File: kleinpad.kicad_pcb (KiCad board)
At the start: 2 copper layers, 79 x 79 mm, 31 parts, among them J1 Conn_01x02, J2 Conn_01x05, SW1 SW_Push, SW2 RotaryEncoder_Switch, U1 SuperMini nRF52840

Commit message: feat: add jlc order place
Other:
- board text added: "JLCJLCJLCJLC"
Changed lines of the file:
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@@
 		)
 		(embedded_fonts no)
+		(model "D:/kicad/kbd-3-final/kicad-packages3D/kbd.3dshapes/MX Series-Cherry Key.step"
+			(offset
+				(xyz 7.3 7.5 6)
+			)
+			(scale
+				(xyz 1 1 1)
+			)
+			(rotate
+				(xyz 90 -180 -0)
+			)
+		)
 	)
 	(footprint "kbd_Parts:Diode_TH_SMD"
@@
 			)
 			(justify left bottom mirror)
+		)
+	)
+	(gr_text "JLCJLCJLCJLC"
+		(at 123.8 63.8 0)
+		(layer "B.SilkS")
+		(effects
+			(font
+				(size 0.8 1)
+				(thickness 0.15)
+				(bold yes)
+			)
+			(justify left bottom mirror)

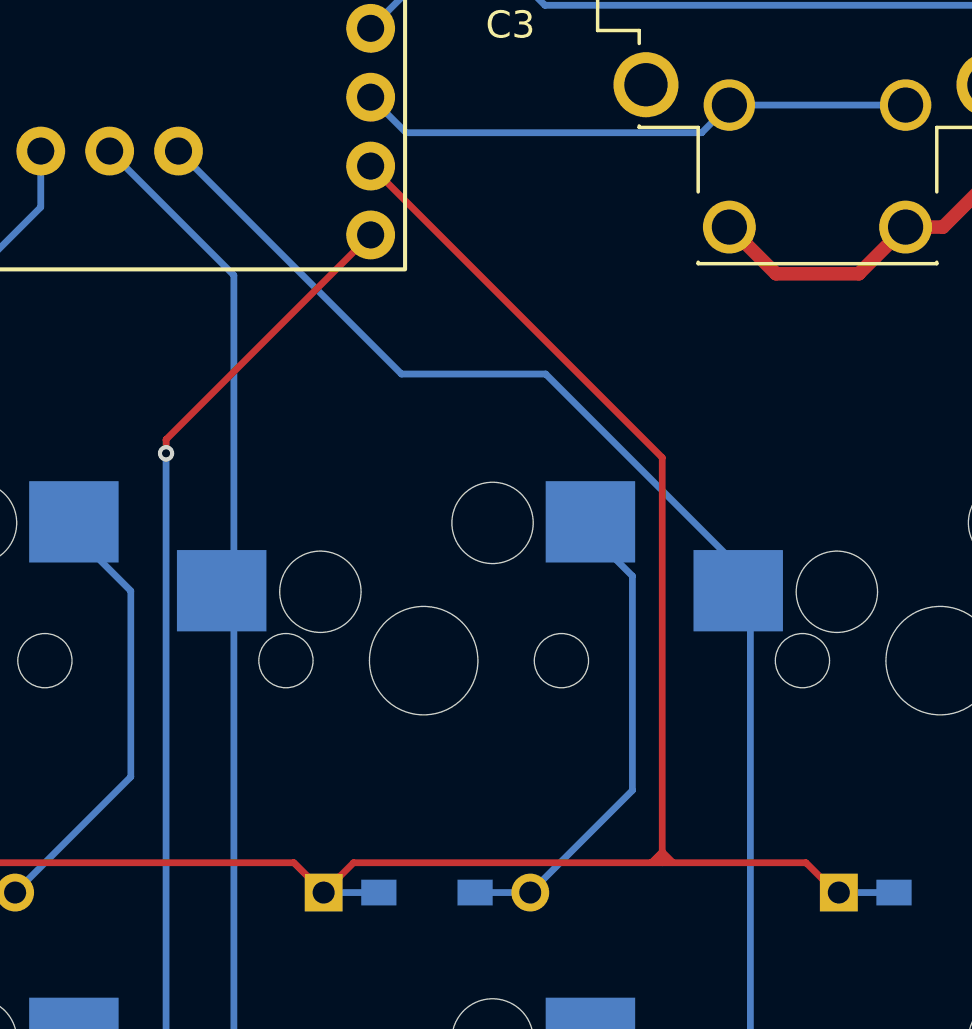
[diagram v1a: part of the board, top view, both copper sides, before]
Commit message: fix: 配線を少しだけ変更
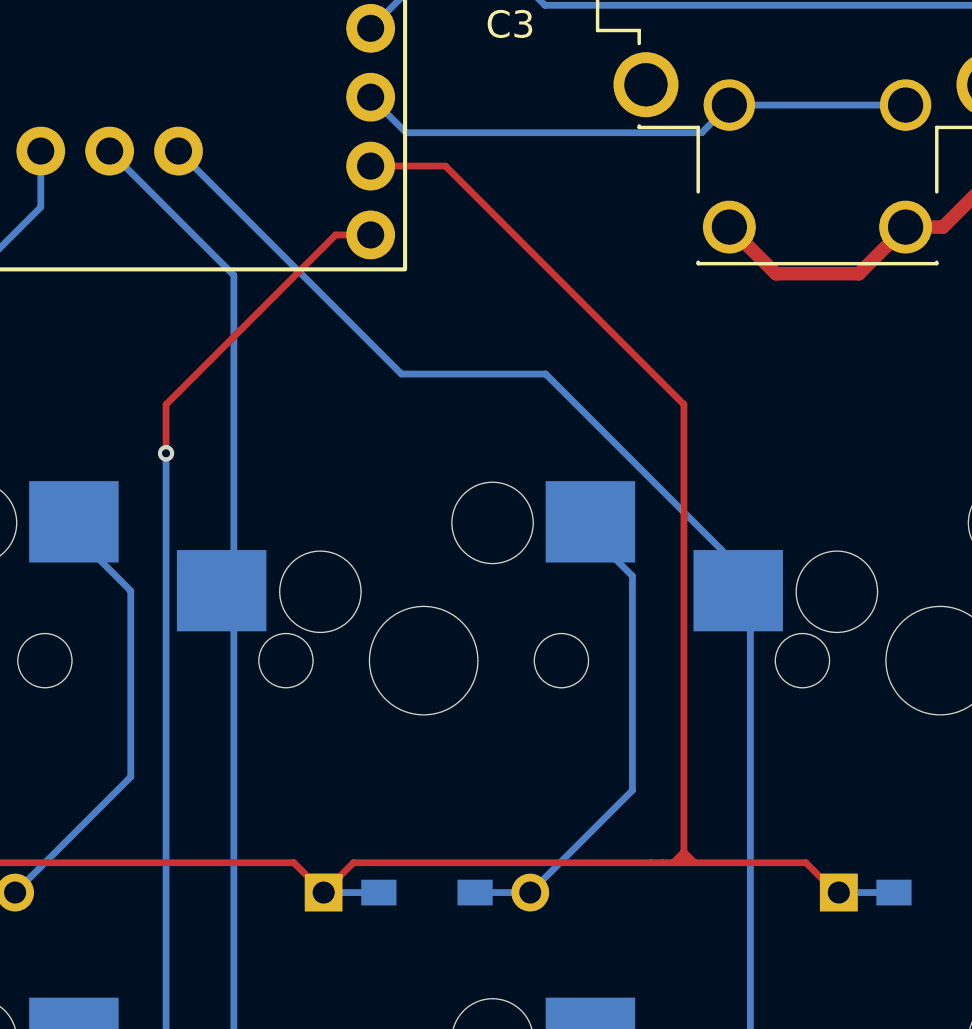
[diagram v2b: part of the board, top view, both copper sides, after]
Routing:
- net ROW_1: track 99.2 -> 101.1 mm
- net ROW_2: track 114.4 -> 115.2 mm
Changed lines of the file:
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@@
-	)
-	(segment
-		(start 159.1 117)
-		(end 159.1 117.4)
-		(width 0.25)
-		(layer "F.Cu")
-		(net 5)
 	)
 	(segment
@@
 	)
 	(segment
-		(start 159.1 117)
+		(start 159.9 117)
 		(end 159.5 117.4)
 		(width 0.25)
@@
 	)
 	(segment
+		(start 159.9 117)
+		(end 160.3 117.4)
+		(width 0.25)
+		(layer "F.Cu")
+		(net 5)
+	)
+	(segment
 		(start 165.5 118.5)
 		(end 164.4 117.4)
@@
 	)
 	(segment
+		(start 159.9 117.4)
+		(end 159.5 117.4)
+		(width 0.25)
+		(layer "F.Cu")
+		(net 5)
+	)
+	(segment
 		(start 164.4 117.4)
-		(end 159.5 117.4)
+		(end 160.3 117.4)
 		(width 0.25)
 		(layer "F.Cu")
@@
 	)
 	(segment
+		(start 159.9 117)
+		(end 159.9 117.4)
+		(width 0.25)
+		(layer "F.Cu")
+		(net 5)
+	)
+	(segment
+		(start 160.3 117.4)
+		(end 159.9 117.4)
+		(width 0.25)
+		(layer "F.Cu")
+		(net 5)
+	)
+	(segment
 		(start 158.7 117.4)
 		(end 147.7125 117.4)
@@
 	)
 	(segment
-		(start 159.1 102.459875)
-		(end 159.1 117)
+		(start 148.345625 91.7055)
+		(end 151.1055 91.7055)
 		(width 0.25)
 		(layer "F.Cu")
@@
 	)
 	(segment
-		(start 159.1 117)
-		(end 158.7 117.4)
-		(width 0.25)
-		(layer "F.Cu")
-		(net 5)
-	)
-	(segment
 		(start 109.7125 117.4)
 		(end 108.6125 118.5)
@@
 	)
 	(segment
+		(start 151.1055 91.7055)
+		(end 159.9 100.5)
+		(width 0.25)
+		(layer "F.Cu")
+		(net 5)
+	)
+	(segment
 		(start 147.7125 117.4)
 		(end 146.6125 118.5)
@@
 	)
 	(segment
-		(start 148.345625 91.7055)
-		(end 159.1 102.459875)
+		(start 159.9 100.5)
+		(end 159.9 117)
 		(width 0.25)
 		(layer "F.Cu")
@@
 	)
 	(segment
+		(start 148.345625 94.2455)
+		(end 147.0545 94.2455)
+		(width 0.25)
+		(layer "F.Cu")
+		(net 7)
+	)
+	(segment
 		(start 127.6125 137.5)
 		(end 126.5125 136.4)
@@
 	)
 	(segment
+		(start 140.8 100.5)
+		(end 140.8 102.3)
+		(width 0.25)
+		(layer "F.Cu")
+		(net 7)
+	)
+	(segment
 		(start 128.7125 136.4)
 		(end 127.6125 137.5)
@@
 	)
 	(segment
-		(start 148.345625 94.2455)
-		(end 140.8 101.791125)
-		(width 0.25)
-		(layer "F.Cu")
-		(net 7)
-	)
-	(segment
 		(start 165.815625 137.5)
 		(end 164.715625 136.4)
@@
 	)
 	(segment
-		(start 140.8 101.791125)
-		(end 140.8 102.3)
-		(width 0.25)
-		(layer "F.Cu")
-		(net 7)
-	)
-	(segment
 		(start 140.8 136.4)
 		(end 140.5 136.4)
@@
 		(width 0.25)
 		(layer "F.Cu")
+		(net 7)
+	)
+	(segment
+		(start 147.0545 94.2455)
+		(end 140.8 100.5)
+		(width 0.25)
+		(layer "F.Cu")
